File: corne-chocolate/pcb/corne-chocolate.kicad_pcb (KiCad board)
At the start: 2 copper layers, 133.8 x 91.4 mm, 98 parts, among them J3 LED, P1 i2c-pin, P2 i2c-pin, SW1 SW_PUSH, SW10 SW_PUSH, SW11 SW_PUSH, SW12 SW_PUSH, SW13 SW_PUSH, SW14 SW_PUSH, SW15 SW_PUSH, SW16 SW_PUSH, SW17 SW_PUSH, SW18 SW_PUSH, SW19 SW_PUSH, SW2 SW_PUSH, SW20 SW_PUSH, SW21 SW_PUSH, SW3 SW_PUSH, SW4 SW_PUSH, SW5 SW_PUSH, SW6 SW_PUSH, SW7 SW_PUSH, SW8 SW_PUSH, SW9 SW_PUSH, U1 ProMicro

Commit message: Update to v2.1
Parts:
- SW1, SW10, SW11, SW12, SW13, SW14, SW15, SW16, SW17, SW18, SW19, SW2, SW20, SW3, SW4, SW5, SW6, SW7, SW8, SW9: footprint kbd:CherryMX_Hotswap -> kbd:Choc_Hotswap
- SW21: footprint kbd:CherryMX_Hotswap_1.5u -> kbd:Choc_Hotswap_1.5u
- moved L27 1.42 mm to (165.0, 122.9)
- moved L24 1.38 mm to (165.0, 84.9)
- moved L26 1.37 mm to (127.0, 118.2)
- moved L23 1.36 mm to (127.0, 80.2)
- moved L22 1.35 mm to (89.0, 87.2)
- moved L25 1.34 mm to (89.0, 106.2)
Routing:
- net VCC: track 759.1 -> 786.4 mm, vias 33 -> 30
- net Net-(D21-Pad2): track 61.1 -> 50.2 mm, vias 3 -> 2
- net col2: track 202.1 -> 193.4 mm, vias 13 -> 11
- net GND: track 823.7 -> 816.7 mm, vias 61 -> 59
- net col4: track 203.2 -> 196.2 mm, vias 11 -> 8
- net Net-(L13-Pad3): track 38.3 -> 31.6 mm
- net Net-(L2-Pad3): track 40.7 -> 46.2 mm, vias 4 -> 6
- net Net-(D5-Pad2): track 25.4 -> 20.2 mm, vias 3 -> 2
- net Net-(D11-Pad2): track 24.7 -> 20.0 mm, vias 3 -> 2
- net row0: track 202.0 -> 197.4 mm
- net col0: track 250.8 -> 255.1 mm, vias 9 -> 12
- net Net-(D17-Pad2): track 24.6 -> 20.3 mm, vias 3 -> 2
- net col3: track 228.9 -> 224.8 mm, vias 13 -> 12
- net Net-(D18-Pad2): track 25.5 -> 21.4 mm
- net Net-(D12-Pad2): track 26.1 -> 22.3 mm, vias 2 -> 3
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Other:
- board text added: "Corne Chocolate v2.1 PCB Designed by foostan"
- board text removed: "Corne Chocolate v2.0 PCB Designed by foostan"

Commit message: fixed typo
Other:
- board text added: "Corne Chocolate v2.1 PCB designed by foostan"
- board text removed: "Corne Chocolate v2.1 PCB Designed by foostan"
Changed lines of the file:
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@@
   (gr_line (start 79.5 105.5) (end 79.51 105.5) (angle 90) (layer Eco2.User) (width 2.5))
   (gr_line (start 79.5 86.75) (end 79.51 86.75) (angle 90) (layer Eco2.User) (width 2.5))
-  (gr_text "Corne Chocolate v2.1\nPCB Designed by foostan" (at 117.55 121.45) (layer B.Mask)
+  (gr_text "Corne Chocolate v2.1\nPCB designed by foostan" (at 117.55 121.45) (layer B.Mask)
     (effects (font (size 1 1) (thickness 0.125)) (justify left mirror))
   )
-  (gr_text "Corne Chocolate v2.1\nPCB Designed by foostan" (at 98.25 121.45) (layer F.Mask)
+  (gr_text "Corne Chocolate v2.1\nPCB designed by foostan" (at 98.25 121.45) (layer F.Mask)
     (effects (font (size 1 1) (thickness 0.125)) (justify left))
   )

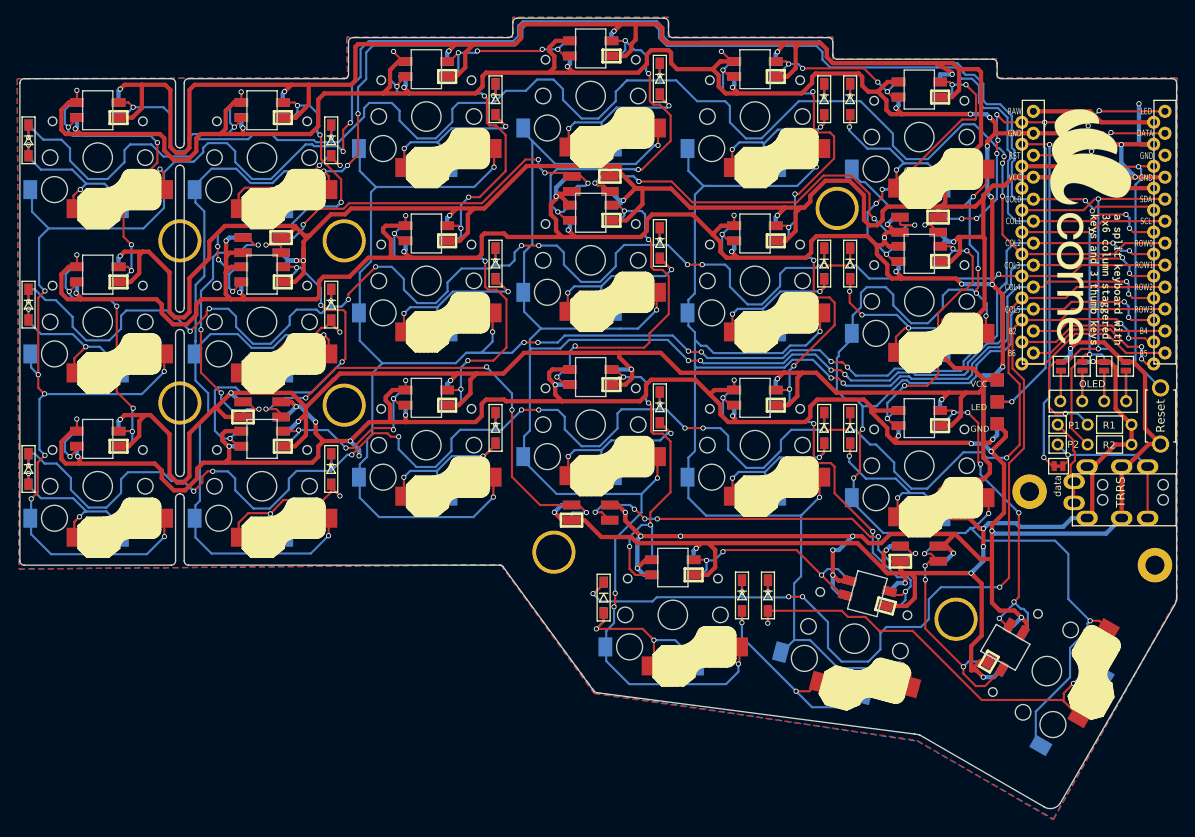
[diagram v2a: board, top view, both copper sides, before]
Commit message: Fix the PCB outline of chocolate
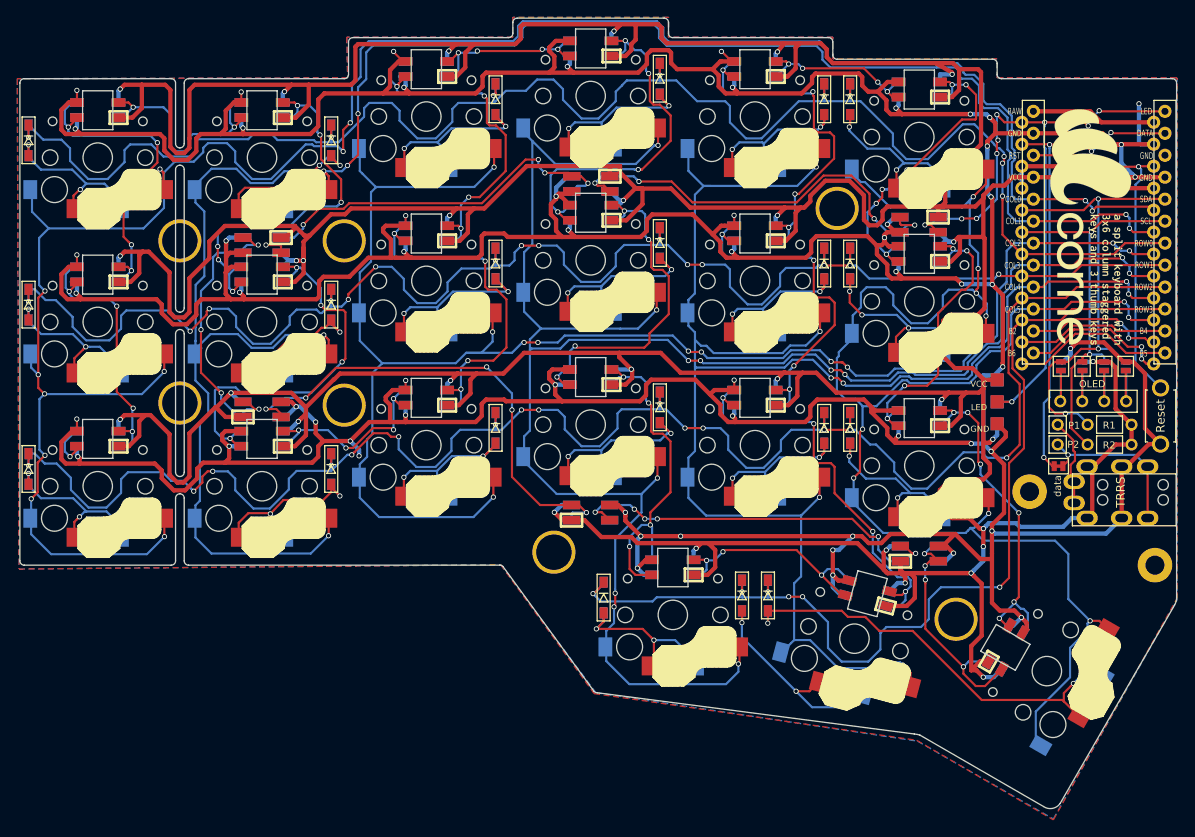
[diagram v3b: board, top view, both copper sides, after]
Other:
- outline, holes or cut-outs redrawn

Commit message: chocolate
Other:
- net class Default removed
